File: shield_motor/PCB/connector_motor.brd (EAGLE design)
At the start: 68.6 x 53.3 mm, 6 parts

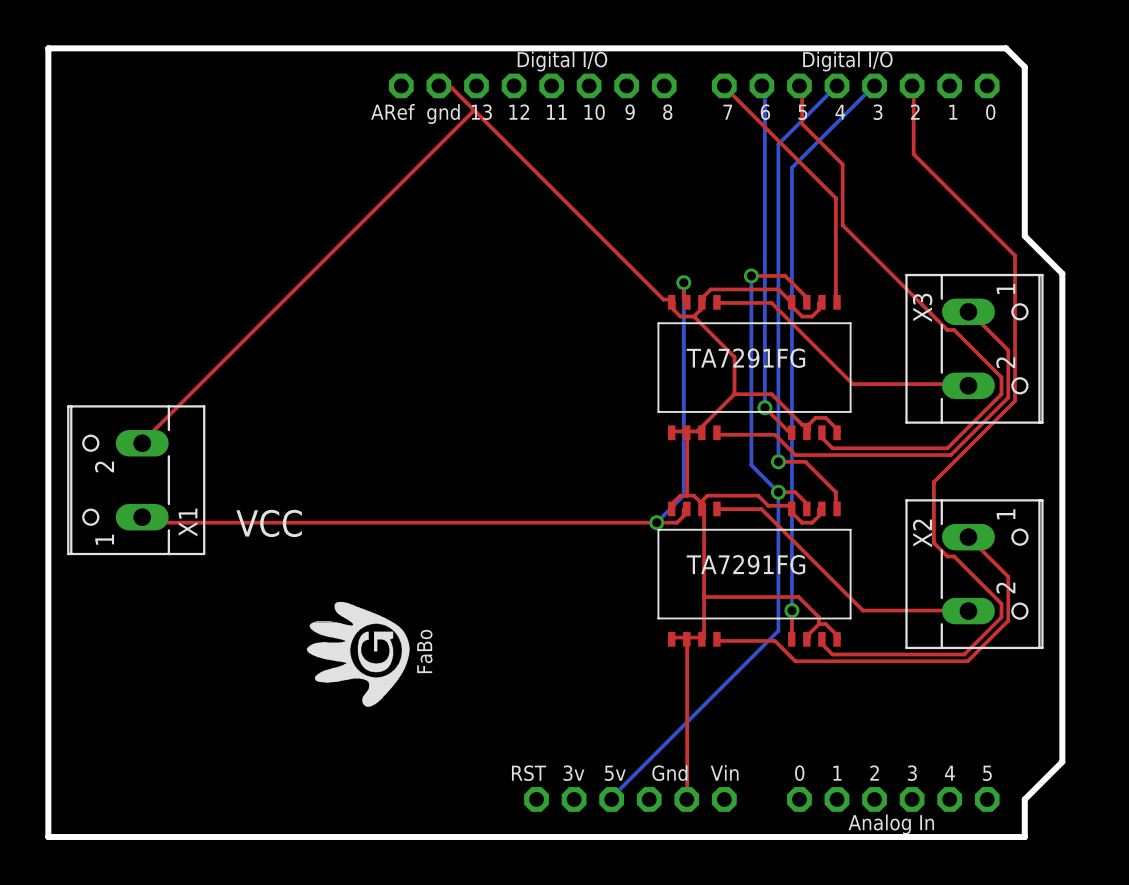
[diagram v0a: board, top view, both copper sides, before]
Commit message: Add 2 another motor drivers
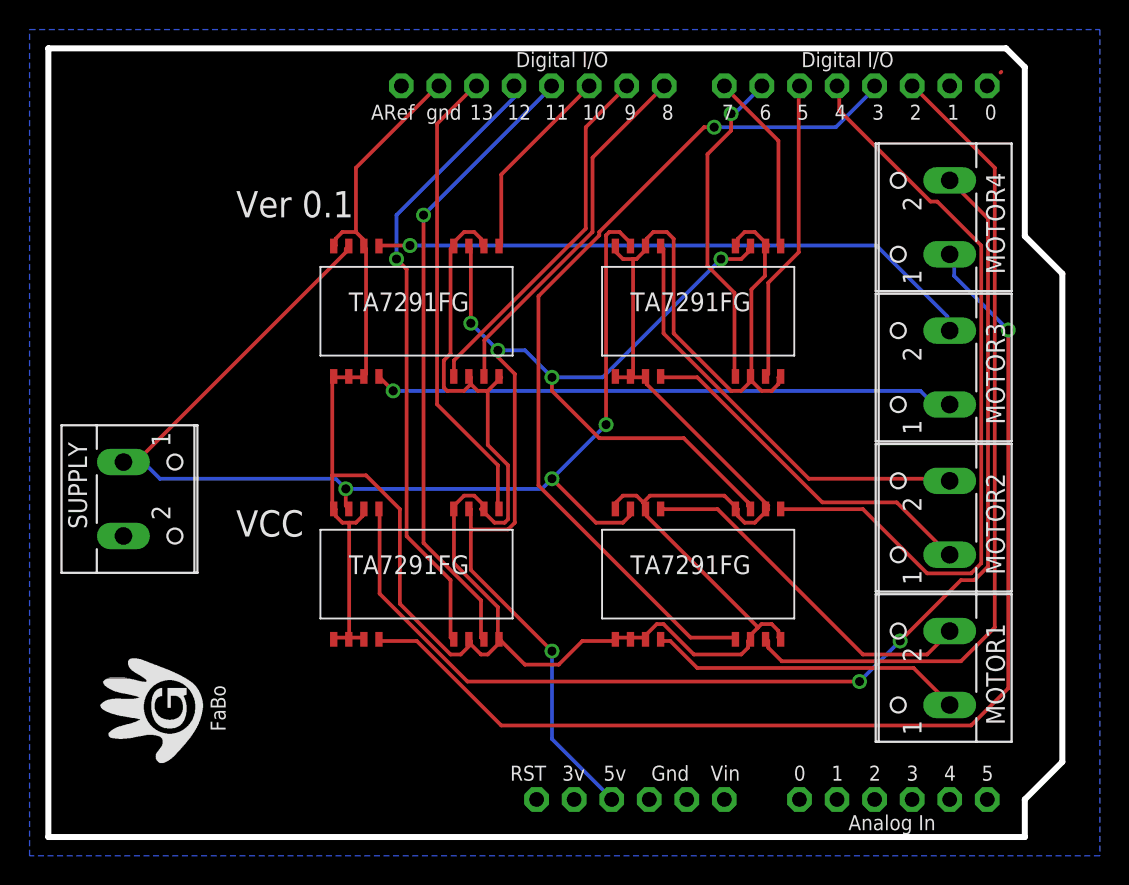
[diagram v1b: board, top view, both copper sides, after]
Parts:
- removed X1, X2, X3: (no value), con-wago-500:W237-102
- added MOTOR1, MOTOR2, MOTOR3, MOTOR4, SUPPLY: (no value), con-wago-500:W237-102
- added U$2, U$5: MOTOR-DRIVER-TA7281FG, gclue:MOTOR-DRIVER-TA7291FG
- moved U$4 5.39 mm to (44.5, 35.6)
- moved U$3 3.81 mm to (44.5, 17.8)
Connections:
- new net M3_IN1: U$1.D8, U$2.7
- new net M3_IN2: U$1.D10, U$2.9
- new net M3_OUT1: MOTOR3.1, U$2.4
- new net M3_OUT2: MOTOR3.2, U$2.13
- new net M3_REF: U$1.D9, U$2.5
- new net M4_IN1: U$1.D11, U$5.7
- new net M4_IN2: U$1.D13, U$5.9
- new net M4_OUT1: MOTOR4.1, U$5.4
- new net M4_OUT2: MOTOR4.2, U$5.13
- new net M4_REF: U$1.D12, U$5.5
- net GND: now also SUPPLY.2, U$2.1, U$2.10, U$2.12, U$2.14, U$2.16, U$2.2, U$2.3, U$2.6, U$2.8, U$5.1, U$5.10, U$5.12, U$5.14, U$5.16, U$5.2, U$5.3, U$5.6, U$5.8; no longer X1.2
- net M1_OUT1: now also MOTOR1.1; no longer X2.1
- net M1_OUT2: now also MOTOR1.2; no longer X2.2
- net M2_OUT1: now also MOTOR2.1; no longer X3.1
- net M2_OUT2: now also MOTOR2.2; no longer X3.2
- net M_VCC: now also SUPPLY.1, U$2.15, U$5.15; no longer X1.1
- net VCC: now also U$2.11, U$5.11
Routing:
- net GND: track 140.8 -> 221.9 mm
- net M4_OUT2: track 0.00 -> 79.8 mm, vias 0 -> 2
- net M4_OUT1: track 0.00 -> 77.0 mm, vias 0 -> 1
- net M4_IN1: track 0.00 -> 42.8 mm, vias 0 -> 1
- net M4_REF: track 0.00 -> 42.4 mm, vias 0 -> 1
- net M3_OUT2: track 0.00 -> 41.5 mm, vias 0 -> 1
- net M3_OUT1: track 0.00 -> 39.4 mm, vias 0 -> 1
- net VCC: track 48.1 -> 86.3 mm, vias 2 -> 5
- net M4_IN2: track 0.00 -> 31.5 mm
- net M3_IN1: track 0.00 -> 24.7 mm
- net M3_REF: track 0.00 -> 24.5 mm
- net M_VCC: track 56.1 -> 80.3 mm, vias 2 -> 3
- net M2_IN1: track 41.1 -> 20.6 mm
- net M1_REF: track 39.8 -> 59.5 mm
- net M1_IN2: track 33.0 -> 52.3 mm, vias 1 -> 0
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- added copper zone on layer 16, net GND
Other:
- board text added: "Ver 0.1"

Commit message: Add connector_motor
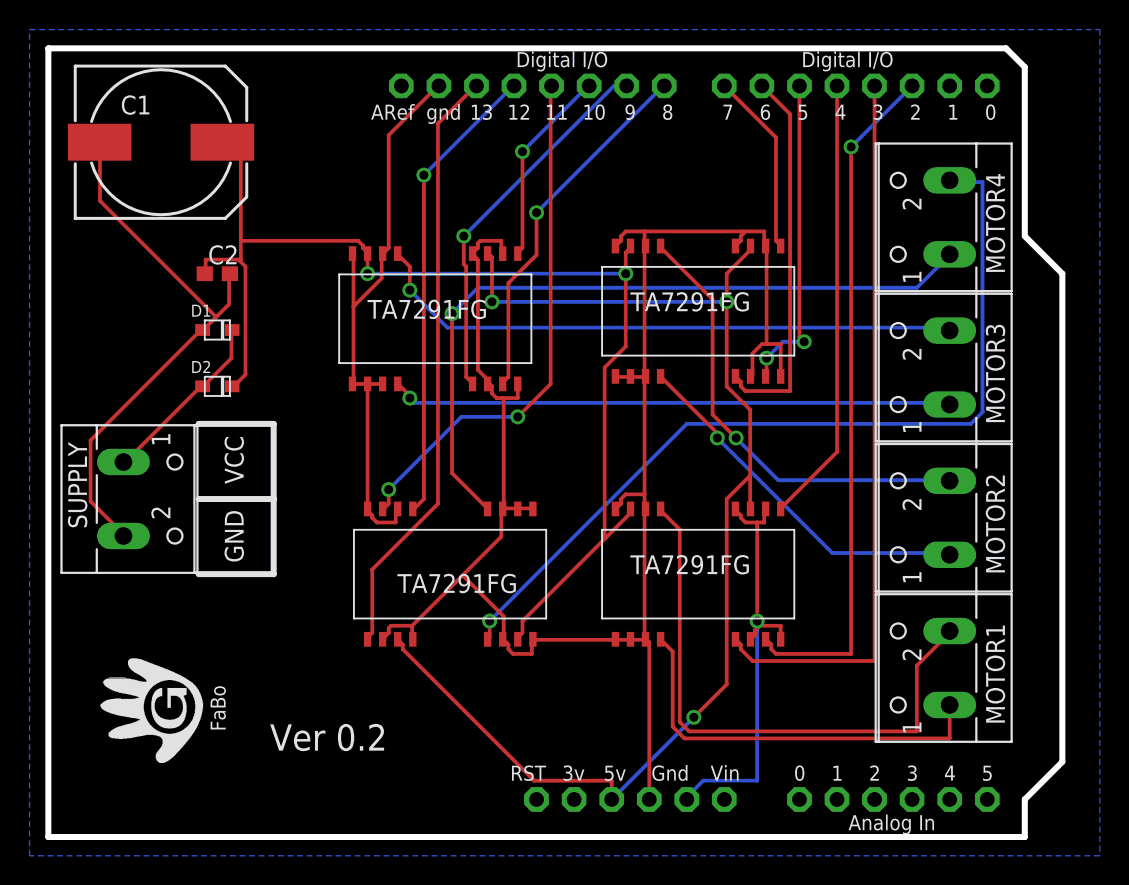
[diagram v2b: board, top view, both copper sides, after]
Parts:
- added C1: 100uf, adafruit:150CLZ-1014
- added C2: 100nf, rcl:C0603
- added D1: (no value), adafruit:SOD-323F
- added D2: 1N4148, adafruit:SOD-323F
- moved U$2 1.37 mm to (26.7, 35.1)
- moved U$5 1.27 mm to (26.7, 17.8), turned to 180 degrees
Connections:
- removed net GND2: U$1.GND2
- new net N$1: D1.C, D2.A, SUPPLY.1
- net GND: now also C1.-, C2.2, D1.A, U$1.GND2
- net M_VCC: now also C1.+, C2.1, D2.C; no longer SUPPLY.1
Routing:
- net M4_OUT1: track 77.0 -> 49.5 mm
- net M1_IN2: track 52.3 -> 30.2 mm
- net M4_OUT2: track 79.8 -> 58.4 mm, vias 2 -> 1
- net M1_OUT2: track 24.3 -> 38.9 mm
- net N$1: track 0.00 -> 12.3 mm
- net GND: track 221.9 -> 233.5 mm, vias 0 -> 1
- net M4_REF: track 42.4 -> 31.5 mm
- net M1_REF: track 59.5 -> 49.1 mm, vias 1 -> 0
- net M1_IN1: track 56.3 -> 46.5 mm, vias 0 -> 1
- net M4_IN2: track 31.5 -> 40.5 mm
- net M4_IN1: track 42.8 -> 35.6 mm, vias 1 -> 2
- net M1_OUT1: track 21.4 -> 27.6 mm
- net M2_REF: track 22.1 -> 25.7 mm, vias 1 -> 0
- net VCC: track 86.3 -> 84.1 mm, vias 5 -> 3
- net M3_OUT1: track 39.4 -> 38.1 mm
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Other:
- board text added: "GND"
- board text added: "Ver 0.2"
- board text removed: "Ver 0.1"

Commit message: Modified brick
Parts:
- turned U$5 to 0 degrees
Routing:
- net GND: track 233.5 -> 0.00 mm, vias 1 -> 0
- net VCC: track 84.1 -> 0.00 mm, vias 3 -> 0
- net M_VCC: track 81.4 -> 0.00 mm, vias 2 -> 0
- net M4_OUT2: track 58.4 -> 0.00 mm, vias 1 -> 0
- net M4_OUT1: track 49.5 -> 0.00 mm, vias 1 -> 0
- net M1_REF: track 49.1 -> 0.00 mm
- net M1_IN1: track 46.5 -> 0.00 mm, vias 1 -> 0
- net M4_IN2: track 40.5 -> 0.00 mm
- net M3_OUT2: track 40.5 -> 0.00 mm, vias 1 -> 0
- net M1_OUT2: track 38.9 -> 0.00 mm
- net M3_OUT1: track 38.1 -> 0.00 mm, vias 1 -> 0
- net M4_IN1: track 35.6 -> 0.00 mm, vias 2 -> 0
- net M4_REF: track 31.5 -> 0.00 mm, vias 1 -> 0
- net M2_OUT2: track 30.8 -> 0.00 mm, vias 1 -> 0
- net M1_IN2: track 30.2 -> 0.00 mm
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
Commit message: Update for elect
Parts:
- removed C1: 100uf, adafruit:150CLZ-1014
- removed D1: (no value), adafruit:SOD-323F
- removed D2: 1N4148, adafruit:SOD-323F
- added C3: 100uf, resistor:153CLV-0405
- added D3, D4: 1N4004, diode:DO41-10
- added U$6: (no value), gclue:LOGO_OSHW_T_M
- added U$7: (no value), gclue:LOGO_FABO_M
- moved C2 11.3 mm to (21.1, 43.9)
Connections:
- net GND: now also C3.-, D4.A; no longer C1.-, D1.A
- net M_VCC: now also C3.+, D3.C; no longer C1.+, D2.C
- net N$1: now also D3.A, D4.C; no longer D1.C, D2.A
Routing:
- net GND: track 0.00 -> 212.1 mm
- net M_VCC: track 0.00 -> 106.7 mm, vias 0 -> 3
- net VCC: track 0.00 -> 86.2 mm, vias 0 -> 6
- net M4_OUT1: track 0.00 -> 81.4 mm, vias 0 -> 1
- net M4_OUT2: track 0.00 -> 60.6 mm, vias 0 -> 1
- net M1_REF: track 0.00 -> 56.9 mm, vias 0 -> 1
- net M1_IN1: track 0.00 -> 55.9 mm
- net M1_IN2: track 0.00 -> 52.7 mm
- net M3_OUT1: track 0.00 -> 43.4 mm, vias 0 -> 2
- net M4_IN1: track 0.00 -> 43.2 mm, vias 0 -> 1
- net M2_REF: track 0.00 -> 42.8 mm, vias 0 -> 1
- net M4_REF: track 0.00 -> 41.6 mm, vias 0 -> 2
- net M3_OUT2: track 0.00 -> 39.5 mm, vias 0 -> 2
- net M2_OUT2: track 0.00 -> 36.6 mm, vias 0 -> 2
- net N$1: track 0.00 -> 33.3 mm
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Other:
- board text added: "Motor Shield Rev.Beta"
- board text removed: "FaBo"

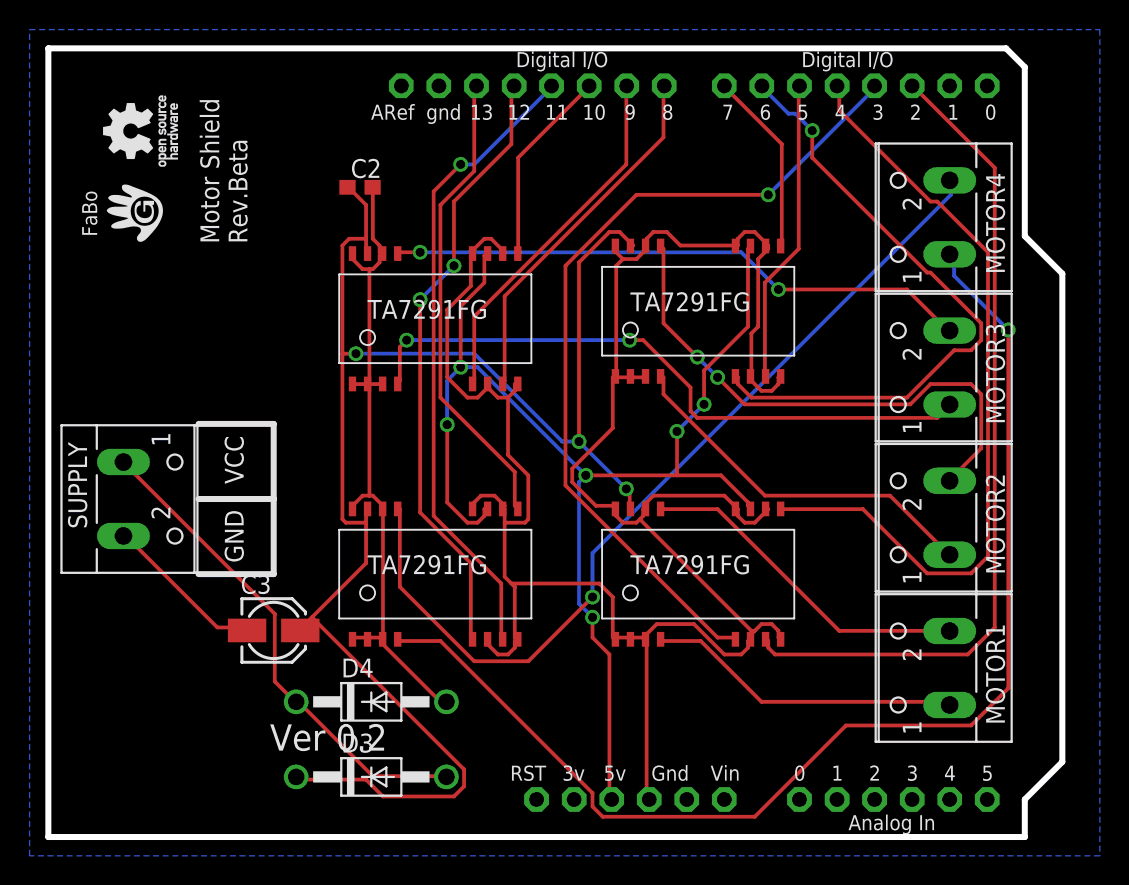
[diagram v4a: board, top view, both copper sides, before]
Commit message: refine board shield_motor
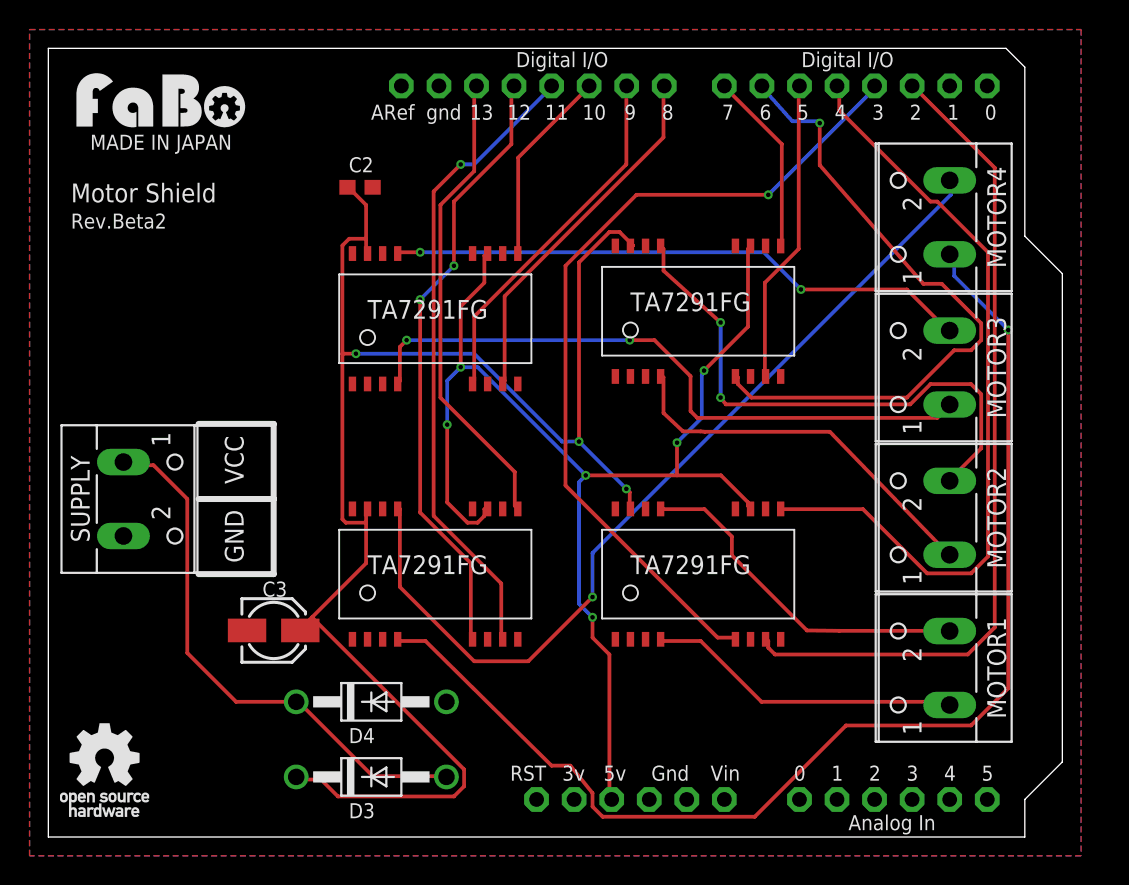
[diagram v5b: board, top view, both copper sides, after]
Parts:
- removed U$6: (no value), gclue:LOGO_OSHW_T_M
- added U$8: (no value), gclue:LOGO_OSHW_T_M
- U$7: device gclue:LOGO_FABO_M -> FaBo:LOGO_FABO_M
- moved U$7 6.11 mm to (7.62, 48.0), turned to 0 degrees
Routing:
- net GND: track 212.1 -> 0.00 mm
- net N$1: track 33.3 -> 36.8 mm
- net M2_REF: track 42.8 -> 43.8 mm
- net M2_OUT2: track 36.6 -> 37.5 mm
- net M2_OUT1: track 25.2 -> 26.0 mm
- net M1_OUT2: track 23.0 -> 23.7 mm
- added copper zone on layer 1, net GND
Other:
- board text added: "MADE IN JAPAN"
- board text added: "Motor Shield"
- board text added: "Rev.Beta2"
- board text removed: "Motor Shield Rev.Beta"
- board text removed: "Ver 0.2"
